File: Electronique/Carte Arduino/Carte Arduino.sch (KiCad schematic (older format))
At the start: 16 parts

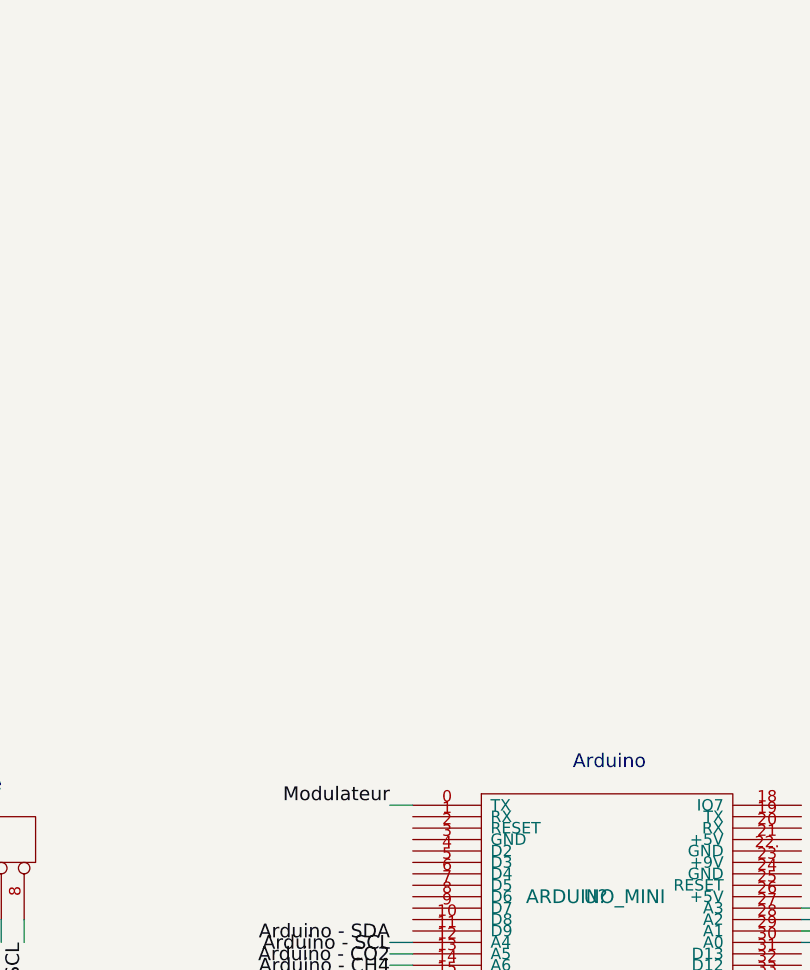
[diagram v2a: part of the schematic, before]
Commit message: Electronique/Carte Arduino/Carte Arduino.sch : - Implémentation du GPS
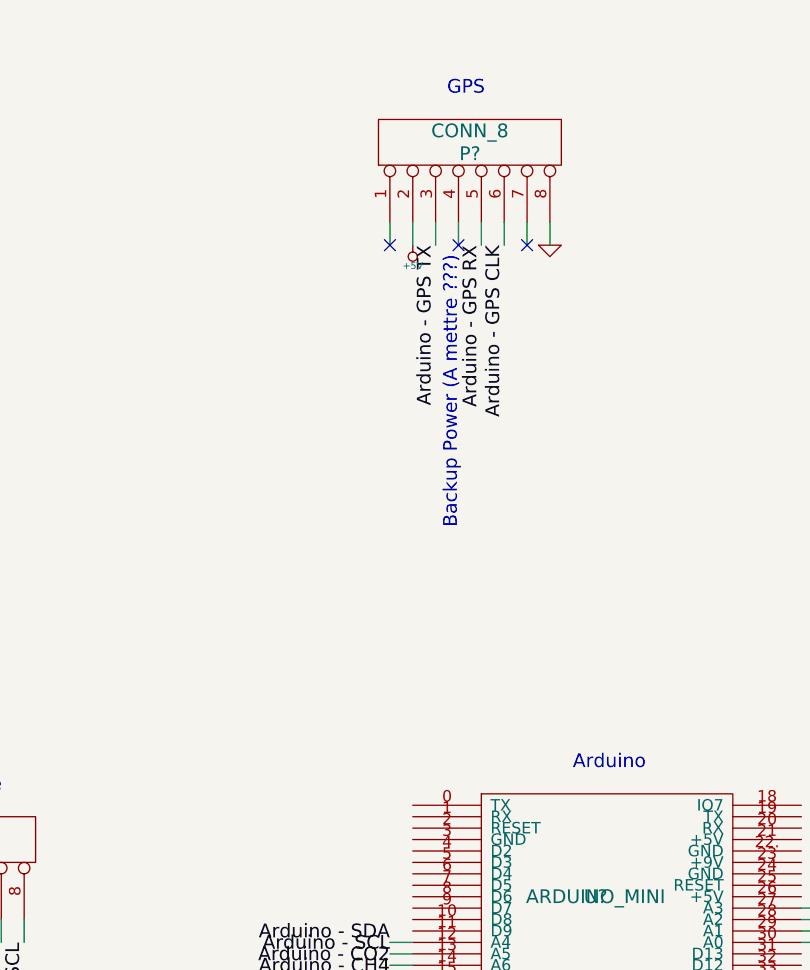
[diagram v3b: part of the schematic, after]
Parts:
- added P?: CONN_8, symbol CONN_8
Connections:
- net +5V: now also P?.2 (P2)
- net GND: now also P?.8 (P8)
- net Modulateur: no longer names the net of U?.0 (TX)
- new net Arduino - GPS CLK: P?.6 (P6)
- new net Arduino - GPS RX: P?.5 (P5)
- new net Arduino - GPS TX: P?.3 (P3)
- no-connect marks 12 -> 15
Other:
- note added: "Backup Power (A mettre ???)"
- note added: "GPS"
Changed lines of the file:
@@
-EESchema Schematic File Version 2  date 13/12/2011 07:36:52
+EESchema Schematic File Version 2  date 13/12/2011 17:36:54
 LIBS:power
 LIBS:device
@@
 Comment4 ""
 $EndDescr
+NoConn ~ 8050 3450
+NoConn ~ 7750 3450
+NoConn ~ 8350 3450
+Text Label 8250 3450 3    60   ~ 0
+Arduino - GPS CLK
+Text Label 8150 3450 3    60   ~ 0
+Arduino - GPS RX
+Text Label 7950 3450 3    60   ~ 0
+Arduino - GPS TX
+Text Notes 8050 3500 3    60   ~ 0
+Backup Power (A mettre ???)
+$Comp
+L GND #PWR?
+U 1 1 4EE77BD6
+P 8450 3450
+F 0 "#PWR?" H 8450 3450 30  0001 C CNN
+F 1 "GND" H 8450 3380 30  0001 C CNN
+	1    8450 3450
+	1    0    0    -1
+$EndComp
+$Comp
+L +5V #PWR?
+U 1 1 4EE77BC5
+P 7850 3450
+F 0 "#PWR?" H 7850 3540 20  0001 C CNN
+F 1 "+5V" H 7850 3540 30  0000 C CNN
+	1    7850 3450
+	-1   0    0    1
+$EndComp
+Wire Wire Line
+	8450 3350 8450 3450
+Wire Wire Line
+	8250 3350 8250 3450
+Wire Wire Line
+	8050 3350 8050 3450
+Wire Wire Line
+	7850 3350 7850 3450
+Wire Wire Line
+	7850 6650 7750 6650
+Wire Wire Line
+	5200 4550 5200 4700
+Wire Wire Line
+	4150 4550 4150 4700
+Wire Wire Line
+	5400 3950 5400 4050
+Wire Wire Line
+	5200 3950 5200 4050
+Wire Wire Line
+	5000 3950 5000 4050
+Wire Wire Line
+	4350 3950 4350 4050
+Wire Wire Line
+	4150 3950 4150 4050
+Wire Wire Line
+	3950 3950 3950 4050
+Wire Wire Line
+	7750 6550 7850 6550
+Wire Wire Line
+	9550 6350 9650 6350
+Wire Wire Line
+	9550 6450 9650 6450
+Wire Wire Line
+	5950 6400 5950 6500
+Wire Wire Line
+	5750 6400 5750 6500
+Wire Wire Line
+	5550 6400 5550 6500
+Wire Wire Line
+	5150 6400 5150 6500
+Wire Wire Line
+	4950 6400 4950 6500
+Wire Wire Line
+	4750 6400 4750 6500
+Wire Wire Line
+	4550 6400 4550 6500
+Wire Wire Line
+	4150 6400 4150 6500
+Wire Wire Line
+	3950 6400 3950 6500
+Wire Wire Line
+	2100 5350 2100 5500
+Wire Wire Line
+	2100 4750 2100 4850
+Wire Wire Line
+	2300 4850 2300 4750
+Wire Wire Line
+	1900 4850 1900 4750
+Wire Wire Line
+	1700 4750 1700 4850
+Wire Wire Line
+	1700 5350 1700 5500
+Wire Wire Line
+	1300 5350 1300 5500
+Wire Wire Line
+	1300 4750 1300 4850
+Wire Wire Line
+	1500 4850 1500 4750
+Wire Wire Line
+	1100 4850 1100 4750
+Wire Wire Line
+	900  4750 900  4850
+Wire Wire Line
+	900  5350 900  5500
+Wire Wire Line
+	3850 6400 3850 6500
+Wire Wire Line
+	4050 6400 4050 6500
+Wire Wire Line
+	4450 6400 4450 6500
+Wire Wire Line
+	4650 6400 4650 6500
+Wire Wire Line
+	4850 6400 4850 6500
+Wire Wire Line
+	5050 6400 5050 6500
+Wire Wire Line
+	5450 6400 5450 6500
+Wire Wire Line
+	5650 6400 5650 6500
+Wire Wire Line
+	5850 6400 5850 6500
+Wire Wire Line
+	6050 6400 6050 6500
+Wire Wire Line
+	6150 6400 6150 6500
+Wire Wire Line
+	9550 6500 9650 6500
+Wire Wire Line
+	9550 6400 9650 6400
+Wire Wire Line
+	7850 6500 7750 6500
+Wire Wire Line
+	3850 3950 3850 4050
+Wire Wire Line
+	4050 3950 4050 4050
+Wire Wire Line
+	4250 3950 4250 4050
+Wire Wire Line
+	4900 3950 4900 4050
+Wire Wire Line
+	5100 3950 5100 4050
+Wire Wire Line
+	5300 3950 5300 4050
+Wire Wire Line
+	7850 6600 7750 6600
+Wire Wire Line
+	7750 3350 7750 3450
+Wire Wire Line
+	7950 3350 7950 3450
+Wire Wire Line
+	8150 3350 8150 3450
+Wire Wire Line
+	8350 3350 8350 3450
+Text Notes 8000 2800 0    60   ~ 0
+GPS
+$Comp
+L CONN_8 P?
+U 1 1 4EE77691
+P 8100 3000
+F 0 "P?" V 8050 3000 60  0000 C CNN
+F 1 "CONN_8" V 8150 3000 60  0000 C CNN
+	1    8100 3000
+	0    -1   -1   0
+$EndComp
 NoConn ~ 5400 4050
 NoConn ~ 5300 4050
 NoConn ~ 4350 4050
 NoConn ~ 4250 4050
-Wire Wire Line
-	7850 6650 7750 6650
-Wire Wire Line
-	5200 4550 5200 4700
-Wire Wire Line
-	4150 4550 4150 4700
-Wire Wire Line
-	5400 3950 5400 4050
-Wire Wire Line
-	5200 3950 5200 4050
-Wire Wire Line
-	5000 3950 5000 4050
-Wire Wire Line
-	4350 3950 4350 4050
-Wire Wire Line
-	4150 3950 4150 4050
-Wire Wire Line
-	3950 3950 3950 4050
-Wire Wire Line
-	7750 6550 7850 6550
-Wire Wire Line
-	9550 6350 9650 6350
-Wire Wire Line
-	9550 6450 9650 6450
-Wire Wire Line
-	7850 5900 7750 5900
-Wire Wire Line
-	5950 6400 5950 6500
-Wire Wire Line
-	5750 6400 5750 6500
-Wire Wire Line
-	5550 6400 5550 6500
-Wire Wire Line
-	5150 6400 5150 6500
-Wire Wire Line
-	4950 6400 4950 6500
-Wire Wire Line
-	4750 6400 4750 6500
-Wire Wire Line
-	4550 6400 4550 6500
-Wire Wire Line
-	4150 6400 4150 6500
-Wire Wire Line
-	3950 6400 3950 6500
-Wire Wire Line
-	2100 5350 2100 5500
-Wire Wire Line
-	2100 4750 2100 4850
-Wire Wire Line
-	2300 4850 2300 4750
-Wire Wire Line
-	1900 4850 1900 4750
-Wire Wire Line
-	1700 4750 1700 4850
-Wire Wire Line
-	1700 5350 1700 5500
-Wire Wire Line
-	1300 5350 1300 5500
-Wire Wire Line
-	1300 4750 1300 4850
-Wire Wire Line
-	1500 4850 1500 4750
-Wire Wire Line
-	1100 4850 1100 4750
-Wire Wire Line
-	900  4750 900  4850
-Wire Wire Line
-	900  5350 900  5500
-Wire Wire Line
-	3850 6400 3850 6500
-Wire Wire Line
-	4050 6400 4050 6500
-Wire Wire Line
-	4450 6400 4450 6500
-Wire Wire Line
-	4650 6400 4650 6500
-Wire Wire Line
-	4850 6400 4850 6500
-Wire Wire Line
-	5050 6400 5050 6500
-Wire Wire Line
-	5450 6400 5450 6500
-Wire Wire Line
-	5650 6400 5650 6500
-Wire Wire Line
-	5850 6400 5850 6500
-Wire Wire Line
-	6050 6400 6050 6500
-Wire Wire Line
-	6150 6400 6150 6500
-Wire Wire Line
-	9550 6500 9650 6500
-Wire Wire Line
-	9550 6400 9650 6400
-Wire Wire Line
-	7850 6500 7750 6500
-Wire Wire Line
-	3850 3950 3850 4050
-Wire Wire Line
-	4050 3950 4050 4050
-Wire Wire Line
-	4250 3950 4250 4050
-Wire Wire Line
-	4900 3950 4900 4050
-Wire Wire Line
-	5100 3950 5100 4050
-Wire Wire Line
-	5300 3950 5300 4050
-Wire Wire Line
-	7850 6600 7750 6600
 Text Label 7750 6650 2    60   ~ 0
 Arduino - CH4
@@
 Text Label 7750 6500 2    60   ~ 0
 Arduino - SDA
-Text Label 7750 5900 2    60   ~ 0
-Modulateur
 Text Label 9650 6350 0    60   ~ 0
 Arduino - Temperature interieure

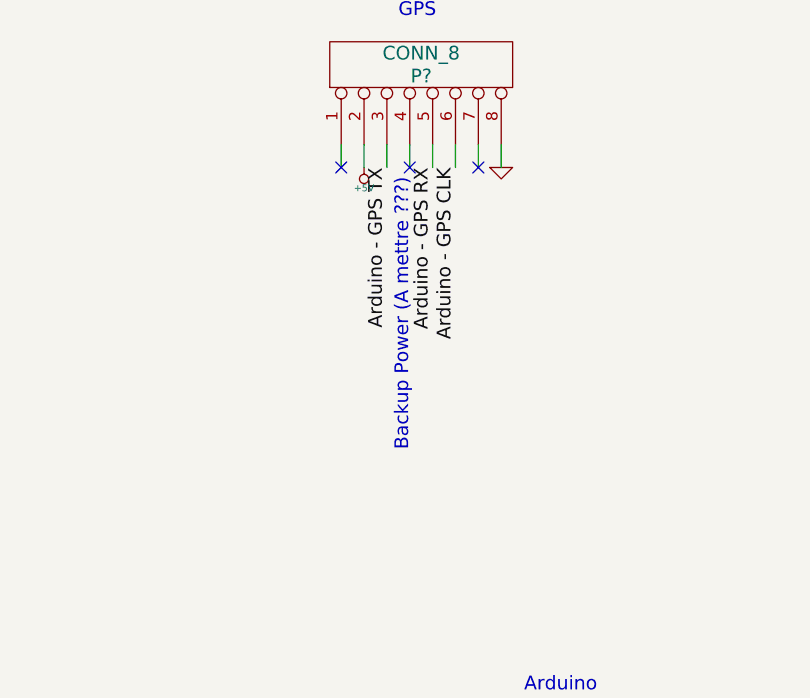
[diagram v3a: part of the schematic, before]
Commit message: Electronique/Carte Arduino/Carte Arduino.sch : - Ajout du Backup power sur le GPS
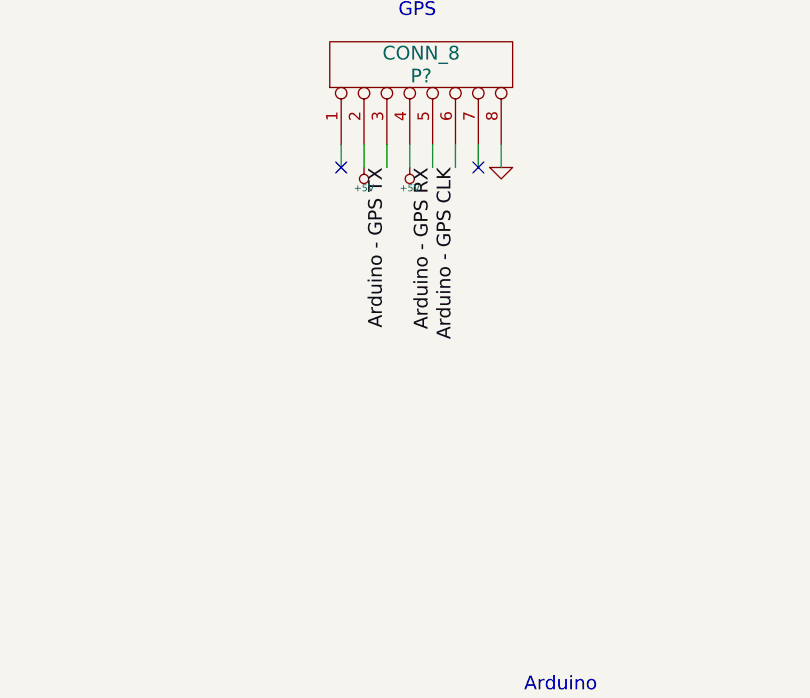
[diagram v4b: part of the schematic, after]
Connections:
- net +5V: now also P?.4 (P4)
- no-connect marks 15 -> 14
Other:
- note removed: "Backup Power (A mettre ???)"
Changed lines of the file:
@@
-EESchema Schematic File Version 2  date 13/12/2011 17:36:54
+EESchema Schematic File Version 2  date 17/12/2011 14:48:52
 LIBS:power
 LIBS:device
@@
 Sheet 1 1
 Title ""
-Date "13 dec 2011"
+Date "17 dec 2011"
 Rev ""
 Comp ""
@@
 Comment4 ""
 $EndDescr
-NoConn ~ 8050 3450
+$Comp
+L +5V #PWR?
+U 1 1 4EEC9DB1
+P 8050 3450
+F 0 "#PWR?" H 8050 3540 20  0001 C CNN
+F 1 "+5V" H 8050 3540 30  0000 C CNN
+	1    8050 3450
+	-1   0    0    1
+$EndComp
 NoConn ~ 7750 3450
 NoConn ~ 8350 3450
@@
 Text Label 7950 3450 3    60   ~ 0
 Arduino - GPS TX
-Text Notes 8050 3500 3    60   ~ 0
-Backup Power (A mettre ???)
 $Comp
 L GND #PWR?

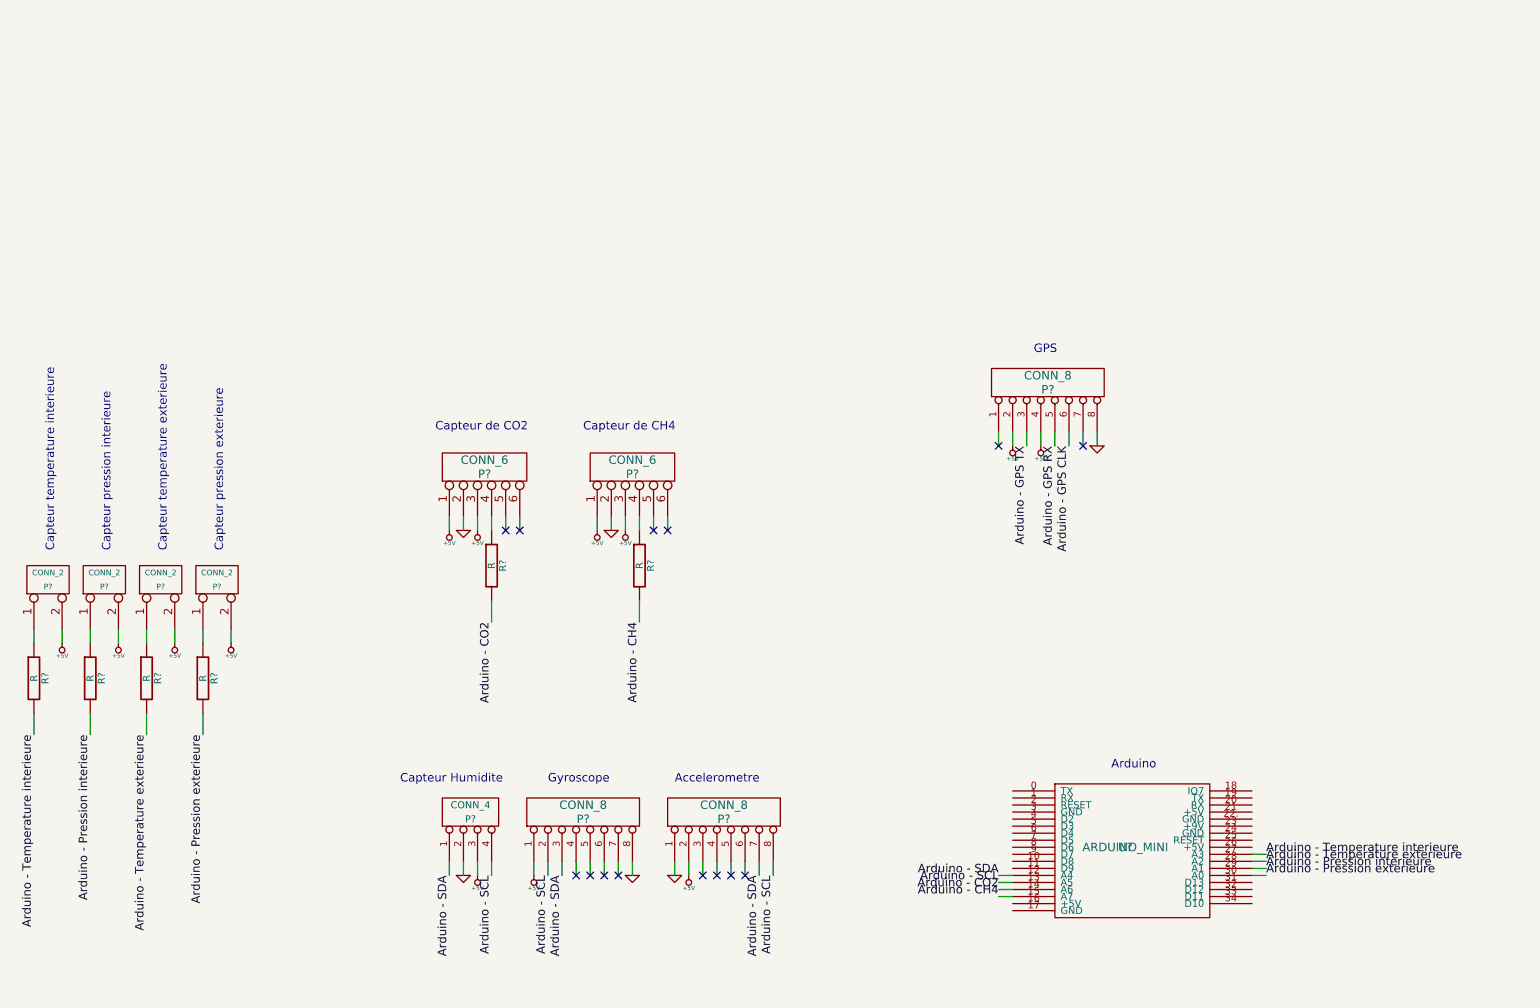
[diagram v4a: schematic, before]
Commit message: Electronique/Carte Arduino/Carte Arduino.sch : - Implémentation des thermistances avec linéarisation
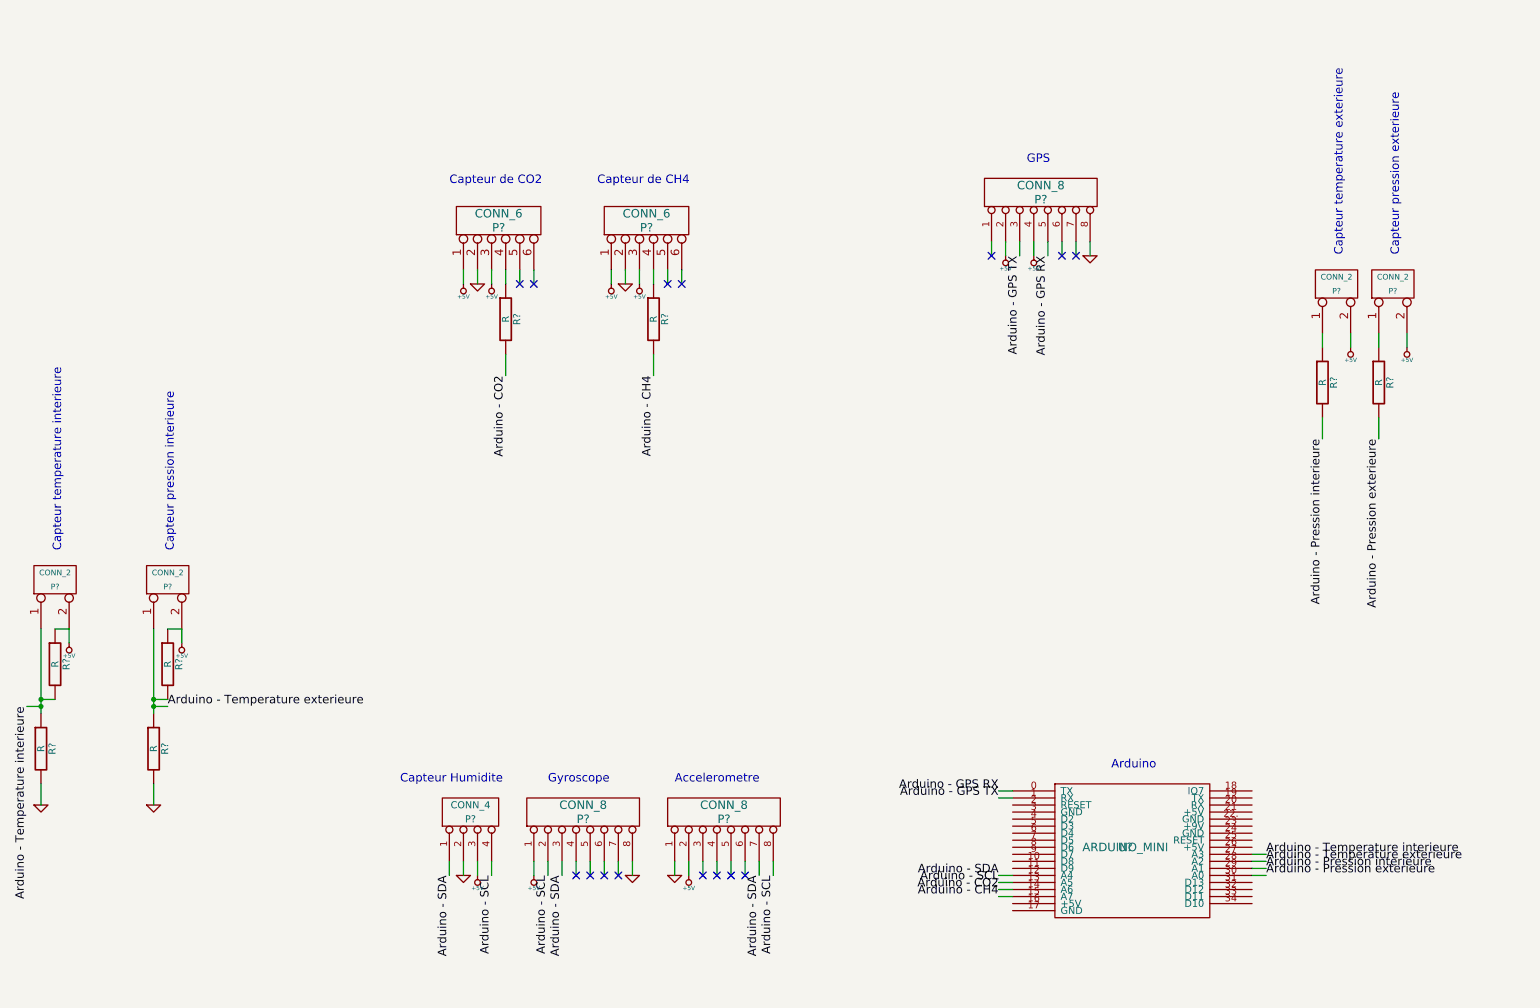
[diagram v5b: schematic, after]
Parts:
- added R? (x2): R, symbol R
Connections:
- net +5V: now also R?.1, R?.1
- net Arduino - GPS RX: now also U?.0 (TX)
- net Arduino - GPS TX: now also U?.1 (RX)
- net Arduino - Pression interieure: now also R?.2; no longer R?.2
- net Arduino - Temperature exterieure: now also P?.1 (P1), R?.1, R?.2; no longer R?.2
- net Arduino - Temperature interieure: now also P?.1 (P1), R?.1, R?.2; no longer R?.2
- net GND: now also R?.2, R?.2
- net Arduino - GPS CLK: no longer names the net of P?.6 (P6)
- no-connect marks 14 -> 15
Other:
- moved on the sheet: P?, R?
